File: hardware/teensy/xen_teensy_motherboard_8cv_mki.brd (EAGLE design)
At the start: 69.9 x 110.5 mm, 359 parts, among them IC1 TL074PW, IC10 TEXAS_INSTRUMENTS_DAC8164IBPW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, IC11 TEXAS_INSTRUMENTS_DAC8164IBPW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, IC12 LM4040-10V, IC2 MCP23S17SO, IC3 MCP6004, IC4 MCP6004, IC5 TL074PW, IC6 TEENSY41-OUTER, IC7 R-78E5.0-0.5, IC8 LM4040-5V, IC9 MCP6004, P1 HEADER/MALE/01NOBORDER, P10 HEADER/MALE/01NOBORDER, P11 HEADER/MALE/01NOBORDER, P12 HEADER/MALE/01NOBORDER, P13 HEADER/MALE/01NOBORDER, P14 HEADER/MALE/01NOBORDER, P15 HEADER/MALE/01NOBORDER, P16 HEADER/MALE/01NOBORDER, P17 HEADER/MALE/01NOBORDER, P18 HEADER/MALE/01NOBORDER, P19 HEADER/MALE/01NOBORDER, P2 HEADER/MALE/01NOBORDER, P20 HEADER/MALE/01NOBORDER, P21 HEADER/MALE/01NOBORDER, P22 HEADER/MALE/01NOBORDER, P23 HEADER/MALE/01NOBORDER, P24 HEADER/MALE/01NOBORDER, P25 HEADER/MALE/01NOBORDER, P26 HEADER/MALE/01NOBORDER, P27 HEADER/MALE/01NOBORDER, P28 HEADER/MALE/01NOBORDER, P29 HEADER/MALE/01NOBORDER, P3 HEADER/MALE/01NOBORDER, P30 HEADER/MALE/01NOBORDER, P31 HEADER/MALE/01NOBORDER, P32 HEADER/MALE/01NOBORDER, P33 HEADER/MALE/01NOBORDER, P34 HEADER/MALE/01NOBORDER, P35 HEADER/MALE/01NOBORDER, P36 HEADER/MALE/01NOBORDER, P37 HEADER/MALE/01NOBORDER, P38 HEADER/MALE/01NOBORDER, P39 HEADER/MALE/01NOBORDER, P4 HEADER/MALE/01NOBORDER, P40 HEADER/MALE/01NOBORDER, P41 HEADER/MALE/01NOBORDER, P42 HEADER/MALE/01NOBORDER, P43 HEADER/MALE/01NOBORDER, P44 HEADER/MALE/01NOBORDER, P45 HEADER/MALE/01NOBORDER, P46 HEADER/MALE/01NOBORDER, P47 HEADER/MALE/01NOBORDER, P48 HEADER/MALE/01NOBORDER, P49 HEADER/MALE/01NOBORDER, P5 HEADER/MALE/01NOBORDER, P50 HEADER/MALE/01NOBORDER, P6 HEADER/MALE/01NOBORDER, P7 HEADER/MALE/01NOBORDER, P8 HEADER/MALE/01NOBORDER, P9 HEADER/MALE/01NOBORDER, Q1 BF170, Q10 BF170, Q11 BF170, Q12 BF170, Q13 BF170, Q14 BF170, Q15 BF170, Q16 BF170, Q2 BF170, Q3 BF170, Q4 BF170, Q5 BF170, Q6 BF170, Q7 BF170, Q8 BF170, Q9 BF170

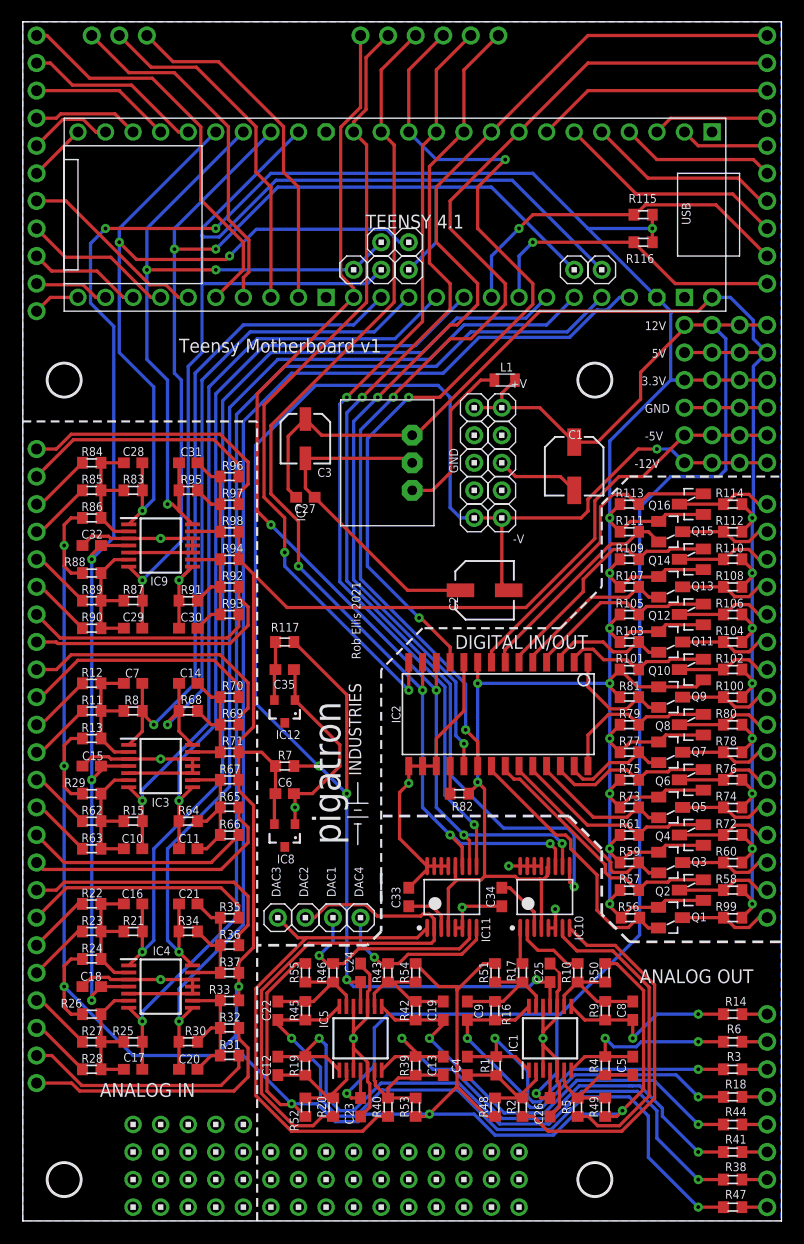
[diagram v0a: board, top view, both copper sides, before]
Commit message: Added Wire.h
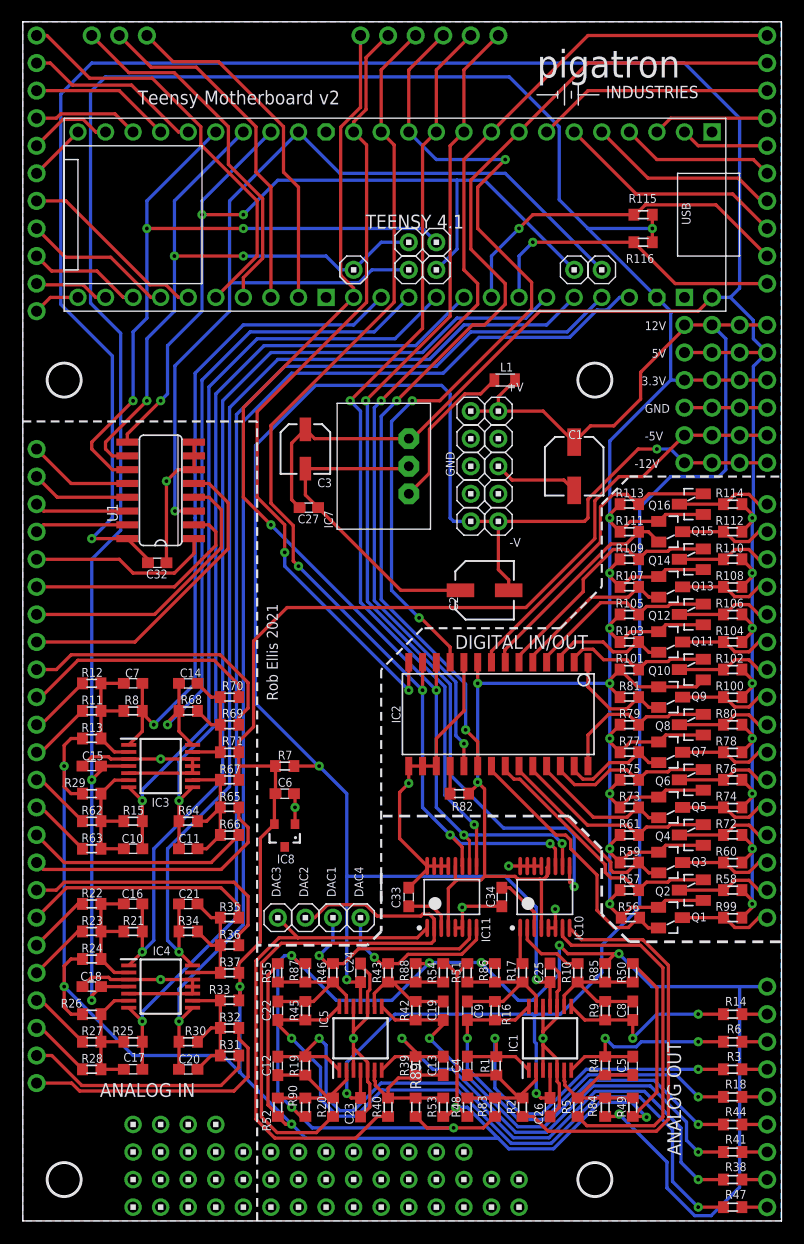
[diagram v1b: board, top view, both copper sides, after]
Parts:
- removed C28, C29, C30, C31: 1nF, capacitors:C0603
- removed C35: 470nF, capacitors:C0603
- removed IC12: LM4040-10V, ic_voltage_reg:SOT-23
- removed IC9: MCP6004, ic_analogue:TSSOP14
- removed P20, P43, P48: HEADER/MALE/01NOBORDER, connectors:HEADER/MALE/01/NOBORDER
- removed R117: 1K, resistors:R0603
- removed R91, R95: 33k, resistors:R0603
- removed R92, R93, R94, R96, R97, R98: 100k, resistors:R0603
- added OFFSET: HEADER/MALE/01, connectors:HEADER/MALE/01
- added U1: 74HC405174HC4051_SO16, ic_analogue:SO16
- R83, R87: value 33k -> 120k
- R84, R85, R86, R88, R89, R90: value 100k -> 120k
- moved R84 75.9 mm to (53.7, 10.5), turned to 90 degrees
- moved U$1 67.4 mm to (56.3, 105.3), turned to 0 degrees
- moved R83 65.9 mm to (43.5, 10.5), turned to 90 degrees
- moved R85 64.9 mm to (53.7, 22.9), turned to 270 degrees
- moved R86 56.0 mm to (43.5, 22.9), turned to 270 degrees
- moved R89 55.4 mm to (36.2, 10.5), turned to 90 degrees
- moved R90 48.3 mm to (26.0, 10.5), turned to 90 degrees
- moved R88 47.4 mm to (36.2, 22.9), turned to 270 degrees
- moved R87 37.8 mm to (26.0, 22.9), turned to 270 degrees
- moved CV1B 10.2 mm to (1.27, 12.7)
- moved CV3B 10.2 mm to (1.27, 22.9)
- moved C32 6.24 mm to (12.4, 60.6), turned to 180 degrees
- moved 24_4.0-A10 2.54 mm to (35.6, 87.6)
- moved 25_4.0-A11 2.54 mm to (38.1, 87.6)
- moved 26_4.0-A12 2.54 mm to (35.6, 90.2)
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- renumbered CV10 to PT5, CV10B to CV6B, CV11 to PT2, CV11B to CV5B, CV12 to PT1, CV12B to CV8B, CV13B to PT3, CV14B to PT7, CV15B to PT8, CV16B to PT4, CV9 to PT6, CV9B to CV7B
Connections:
- removed net -10VREF: C35.2, IC12.2, R117.1
- removed net N$102: PT6.1, R92.1
- removed net N$103: C30.1, IC9.9, R91.1, R92.2, R93.2, R94.2
- removed net N$75: C28.1, IC9.2, R83.1, R84.2, R85.2, R86.2
- removed net N$76: PT3.1, R85.1
- removed net N$77: PT2.1, R84.1
- removed net N$78: C29.1, IC9.6, R87.1, R88.2, R89.2, R90.2
- removed net N$79: PT5.1, R89.1
- removed net N$80: PT7.1, R90.1
- removed net N$81: C31.1, IC9.13, R95.1, R96.2, R97.2, R98.2
- removed net N$82: PT1.1, R96.1
- removed net N$83: PT4.1, R97.1
- removed net N$84: PT8.1, R93.1
- new net N$41: PT1.1, U1.13
- new net N$52: PT2.1, U1.14
- new net N$54: PT3.1, U1.15
- new net N$56: PT4.1, U1.12
- new net N$59: PT5.1, U1.1
- new net N$62: PT6.1, U1.5
- new net N$64: PT7.1, U1.2
- new net N$66: PT8.1, U1.4
- new net OFFSET: OFFSET.1, R83.1, R84.1, R85.1, R86.1, R87.1, R88.1, R89.1, R90.1
- net -12V: no longer R117.2
- net -5VREF: no longer R86.1, R88.1, R94.1, R98.1
- net 3.3V: no longer C32.2, IC9.4
- net 5V: now also C32.2, U1.16
- net ADC10: now also U1.10; no longer C31.2, IC9.14, R95.2
- net ADC11: now also U1.11; no longer C28.2, IC9.1, R83.2
- net ADC8: now also U1.3; no longer C30.2, IC9.8, R91.2
- net ADC9: now also U1.9; no longer C29.2, IC9.7, R87.2
- net N$12: now also R86.2
- net N$2: now also R83.2
- net N$20: now also R90.2
- net N$27: now also CV3B.1; no longer CV1B.1
- net N$28: now also R89.2
- net N$34: now also CV1B.1; no longer CV3B.1
- net N$43: now also R88.2
- net N$48: now also R87.2
- net N$5: now also R84.2
- net N$9: now also R85.2
- net PE: now also U1.6, U1.7, U1.8; no longer C35.1, IC12.1, IC9.10, IC9.11, IC9.12, IC9.3, IC9.5
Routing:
- net OFFSET: track 0.00 -> 137.8 mm, vias 0 -> 8
- net 5V: track 145.3 -> 277.8 mm, vias 8 -> 9
- net -5VREF: track 305.8 -> 259.8 mm, vias 7 -> 6
- net N$62: track 0.00 -> 29.3 mm
- net N$66: track 0.00 -> 26.1 mm
- net N$83: track 25.3 -> 0.00 mm
- net N$102: track 24.1 -> 0.00 mm
- net N$82: track 22.1 -> 0.00 mm
- net ADC9: track 103.9 -> 82.1 mm
- net N$64: track 0.00 -> 21.6 mm
- net PE: track 199.4 -> 178.0 mm
- net N$84: track 21.1 -> 0.00 mm
- net ADC8: track 111.6 -> 91.6 mm
- net N$59: track 0.00 -> 17.1 mm
- net 3.3V: track 367.0 -> 382.8 mm, vias 16 -> 13
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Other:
- board text added: "Teensy Motherboard v2"
- board text removed: "Teensy Motherboard v1"

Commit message: Fixed bug setting index to 0
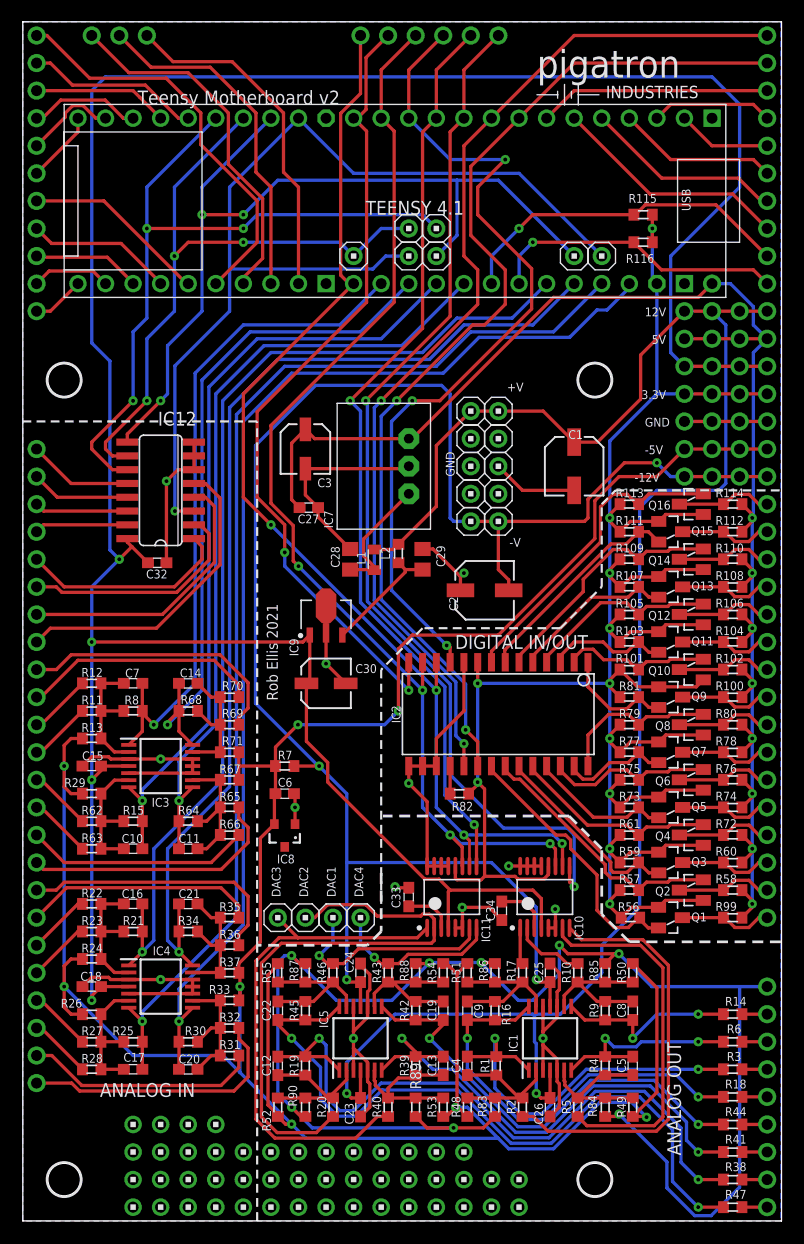
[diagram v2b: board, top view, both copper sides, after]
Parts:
- added 3.3VA, 3.3VA1, 3.3VA2, 3.3VA3: HEADER/MALE/01, connectors:HEADER/MALE/01
- added C28, C29: 22uF, capacitors:C0805
- added C30: 10uF, capacitors:SV-B
- added IC9: 3.3V, ic_voltage_reg:LD2981-SOT89
- added L2: (no value), resistors:R0603
- IC12: value 74HC405174HC4051_SO16 -> CD4051CD4051_SO16
- moved L1 20.4 mm to (32.4, 61.0), turned to 270 degrees
- moved 24_4.0-A10 1.27 mm to (35.6, 88.9)
- moved 24_LC-A10 1.27 mm to (53.3, 88.9)
- moved 25_4.0-A11 1.27 mm to (38.1, 88.9)
- moved 25_LC-A11 1.27 mm to (50.8, 88.9)
- moved 26_LC-A12 1.27 mm to (30.5, 88.9)
- moved GND6 1.27 mm to (63.5, 73.7)
- moved GND7 1.27 mm to (61.0, 73.7)
- moved GND8 1.27 mm to (66.0, 73.7)
- moved GND9 1.27 mm to (68.6, 73.7)
- moved IC6 1.27 mm to (33.0, 94.0)
- moved C34 1.27 mm to (44.1, 28.6)
- moved +V1 1.27 mm to (63.5, 83.8)
- moved +V3 1.27 mm to (61.0, 83.8)
- moved +V4 1.27 mm to (66.0, 83.8)
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- renumbered U1 to IC12
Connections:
- new net 3.3V_A: 3.3VA.1, 3.3VA1.1, 3.3VA2.1, 3.3VA3.1, C15.2, C18.2, C30.+, C32.2, IC10.4, IC11.4, IC12.16, IC3.4, IC4.4, IC9.1
- new net N$72: C29.2, IC9.3, L2.2
- net +12V: now also L2.1
- net 3.3V: no longer C15.2, C18.2, IC10.4, IC11.4, IC3.4, IC4.4
- net 5V: no longer C32.2, IC12.16
- net N$51: now also C28.2
- net PE: now also C28.1, C29.1, C30.-, IC9.2, IC9.2-2
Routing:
- net 3.3V_A: track 0.00 -> 260.4 mm, vias 0 -> 4
- net 3.3V: track 382.8 -> 214.8 mm, vias 13 -> 11
- net 5V: track 277.8 -> 146.8 mm, vias 9 -> 8
- net +12V: track 150.9 -> 168.1 mm
- net N$72: track 0.00 -> 10.9 mm
- net -5VREF: track 259.8 -> 255.6 mm, vias 6 -> 8
- net N$51: track 14.6 -> 11.4 mm
- net N$41: track 17.1 -> 19.6 mm
- net ADC11: track 65.2 -> 67.0 mm
- net ADC10: track 59.9 -> 61.7 mm
- net PE: track 178.0 -> 179.6 mm, vias 10 -> 13
- net N$46: track 28.8 -> 27.5 mm
- net N$45: track 33.1 -> 31.8 mm
- net N$112: track 5.39 -> 6.66 mm
- net ADC8: track 91.6 -> 92.9 mm
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
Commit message: Updated hardware
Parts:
- added R91, R92, R93, R94: 0R, resistors:R0603
- moved PT4 7.62 mm to (1.27, 63.5)
- moved PT6 5.08 mm to (1.27, 58.4)
- moved PT1 2.54 mm to (1.27, 71.1)
- moved PT3 2.54 mm to (1.27, 66.0)
- moved PT7 2.54 mm to (1.27, 55.9)
- moved PT8 2.54 mm to (1.27, 53.3)
- moved PT2 2.54 mm to (1.27, 68.6)
- moved IC12 1.27 mm to (14.0, 67.3)
- moved C32 1.27 mm to (13.7, 60.6)
- moved U$1 1.27 mm to (56.3, 106.6)
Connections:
- net ADC10: now also R93.2
- net ADC11: now also R94.2
- net ADC8: now also R91.2
- net ADC9: now also R92.2
- net N$52: now also PT8.1; no longer PT6.1
- net N$54: now also PT1.1, R94.1; no longer PT4.1
- net N$56: now also PT4.1, R91.1; no longer PT3.1
- net N$59: now also PT2.1, R93.1; no longer PT1.1
- net N$62: now also PT3.1, R92.1; no longer PT2.1
- net N$64: now also PT6.1; no longer PT7.1
- net N$66: now also PT7.1; no longer PT8.1
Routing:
- net ADC9: track 81.6 -> 95.1 mm, vias 3 -> 4
- net ADC10: track 61.7 -> 72.2 mm, vias 3 -> 4
- net ADC8: track 92.9 -> 103.0 mm, vias 1 -> 2
- net 3.3V_A: track 260.4 -> 266.7 mm
- net N$64: track 21.5 -> 27.1 mm
- net N$41: track 19.6 -> 24.2 mm
- net N$52: track 28.9 -> 33.5 mm
- net N$66: track 25.8 -> 29.6 mm
- net PE: track 179.6 -> 181.8 mm
- net N$56: track 8.62 -> 10.7 mm
- net N$62: track 8.62 -> 10.4 mm
- net ADC11: track 67.0 -> 68.6 mm
- net N$59: track 9.15 -> 10.4 mm
- net N$54: track 9.67 -> 10.9 mm
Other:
- board text added: "3.3VA"

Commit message: update docs
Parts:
- IC10, IC11: value TEXAS_INSTRUMENTS_DAC8164IBPWG4TEXAS_INSTRUMENTS_DAC8164IBPWG4_0_1 -> DAC8164
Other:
- board text added: "Bead"
- board text added: "DAC8164"

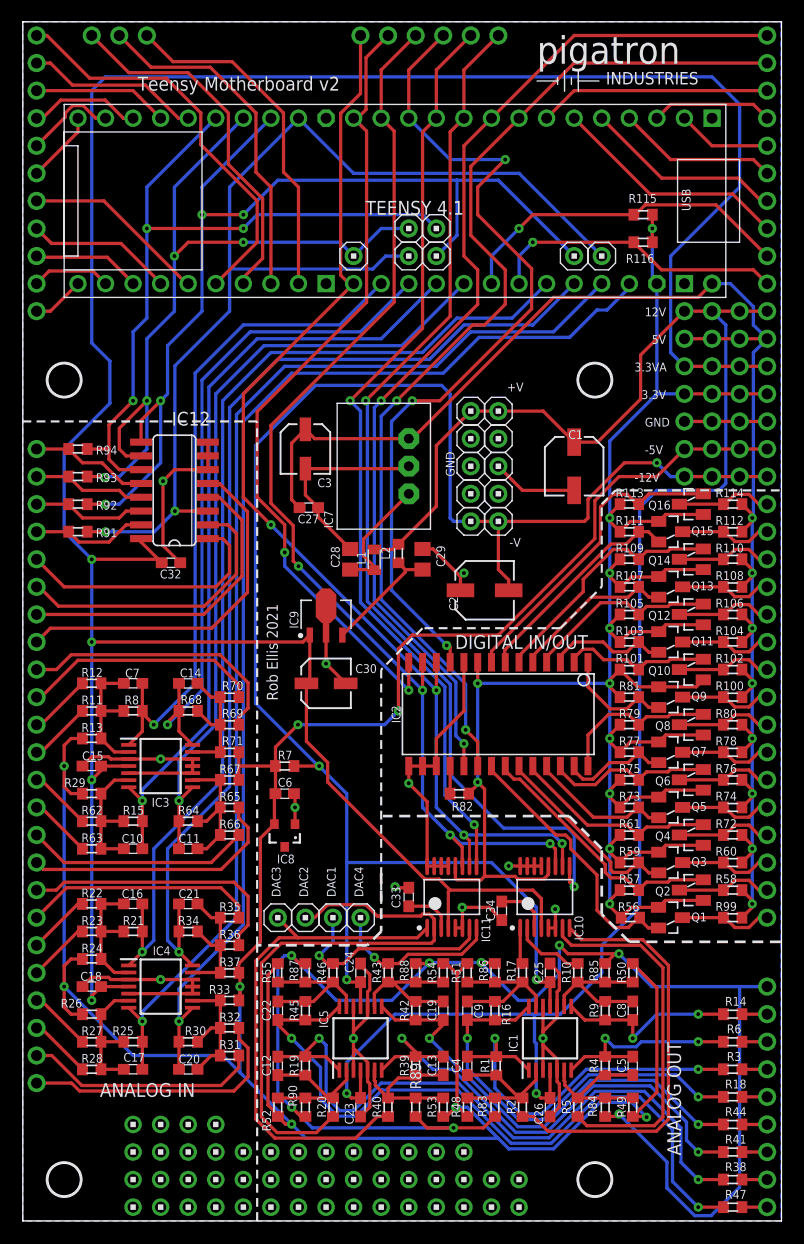
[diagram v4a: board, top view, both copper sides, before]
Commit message: changed  traces
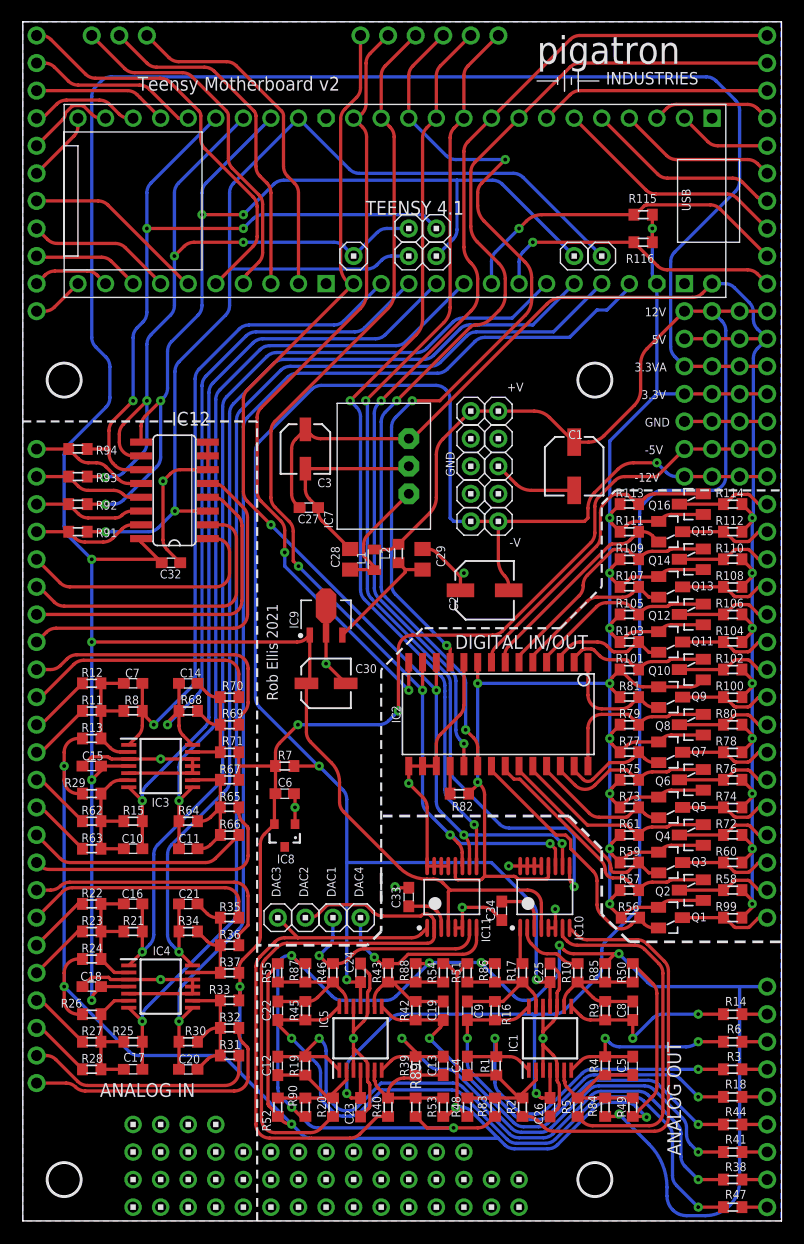
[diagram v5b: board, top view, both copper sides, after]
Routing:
- net -5VREF: track 255.6 -> 252.5 mm
- net 3.3V: track 214.8 -> 212.7 mm
- net +12V: track 168.1 -> 166.1 mm
- net PE: track 181.8 -> 180.4 mm
- net 3.3V_A: track 266.7 -> 265.4 mm
- net N$66: track 29.6 -> 30.7 mm
- net -12V: track 160.0 -> 158.9 mm
- net ADC10: track 72.2 -> 71.1 mm
- net INTA: track 96.9 -> 95.9 mm
- net N$49: track 64.7 -> 63.7 mm
- net N$52: track 33.5 -> 34.4 mm
- net N$21: track 61.3 -> 60.5 mm
- net SPI_IO_CS: track 78.0 -> 77.1 mm
- net INTB: track 97.2 -> 96.3 mm
- net ADC9: track 95.1 -> 94.3 mm
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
